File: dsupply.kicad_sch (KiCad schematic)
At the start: 67 parts, among them J5 Barrel_Jack, Q10 BC857, Q2 BSS138, Q3 BSS138, Q4 BC857, Q5 AOSP21321, Q6 BC857, Q8 BC857, Q9 AOSP21321, U21 ACPL-217-500E, U22 TPS54620, U24 PM1202, U25 AMS1117-3.3

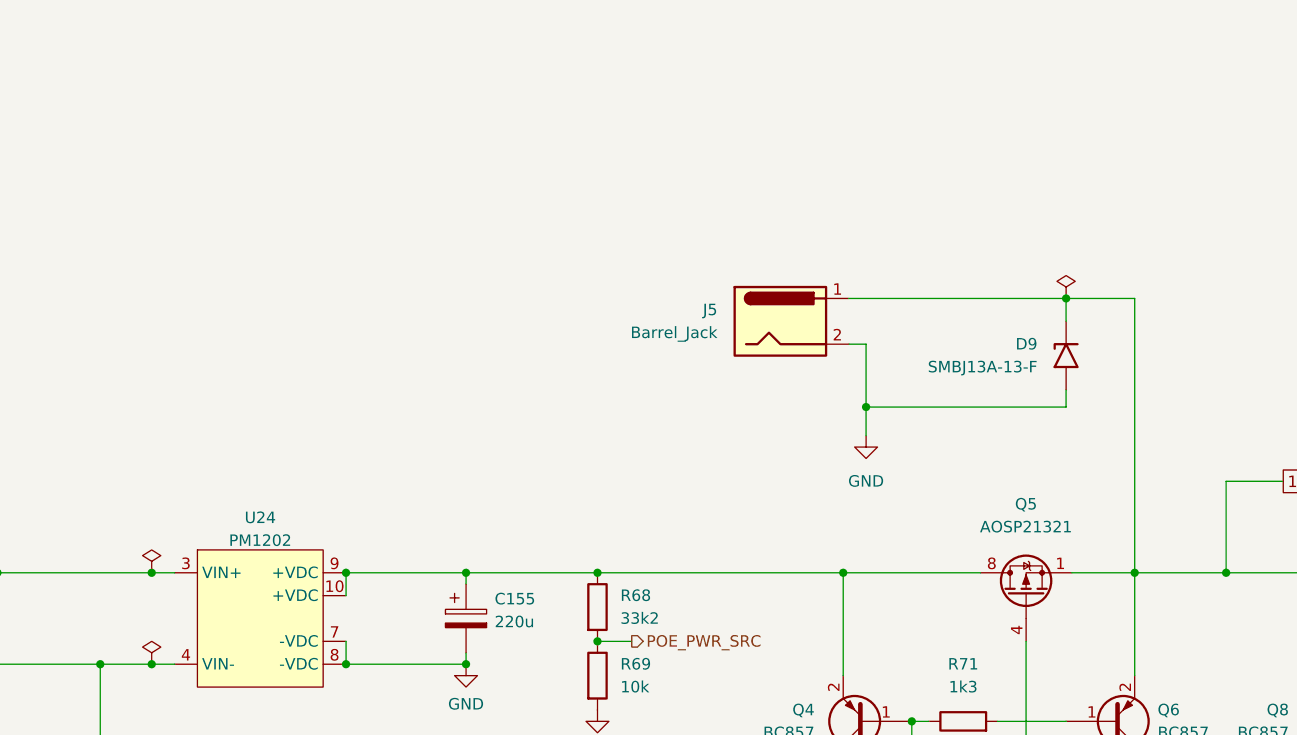
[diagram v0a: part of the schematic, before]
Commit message: sch: Add soft start to 12V PWR Jack input
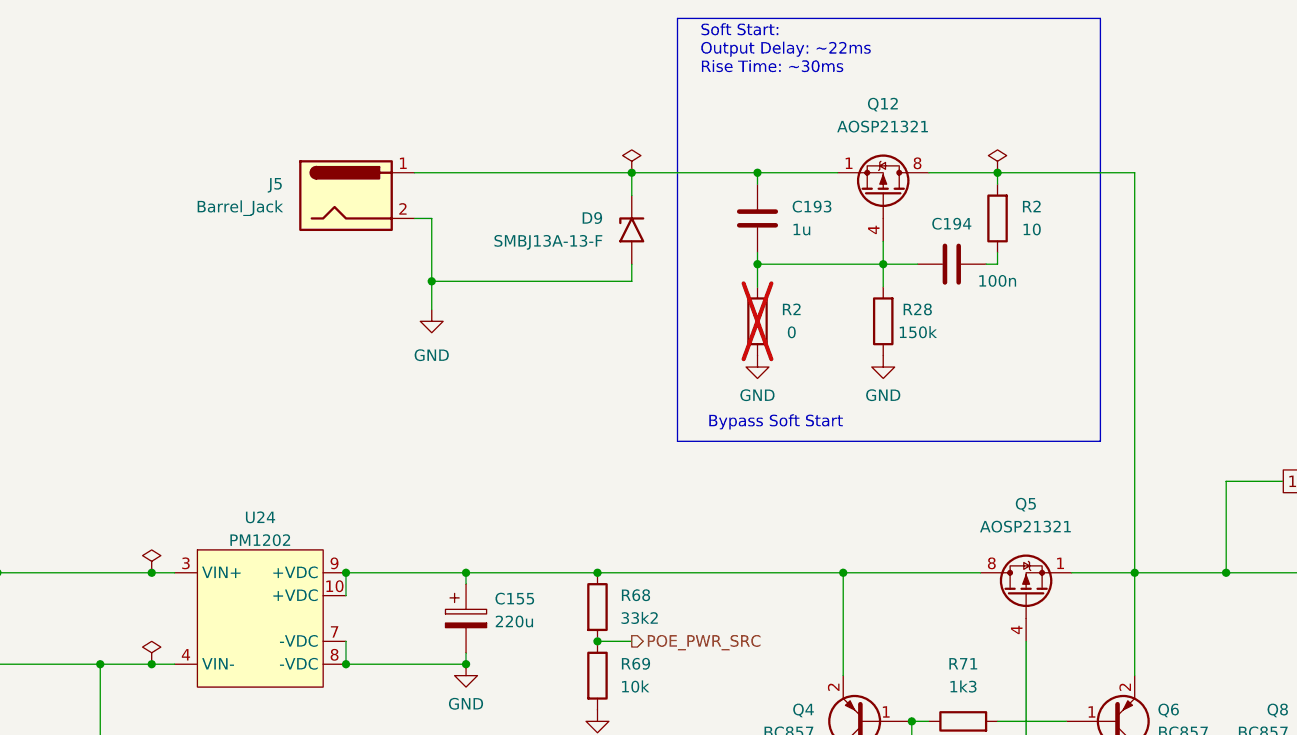
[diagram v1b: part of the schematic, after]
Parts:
- added C193: 1u, Capacitor_SMD:C_0603_1608Metric, symbol Device:C
- added C194: 100n, Capacitor_SMD:C_0603_1608Metric, symbol Device:C
- added Q12: AOSP21321, Package_SO:SOIC-8_3.9x4.9mm_P1.27mm, symbol Transistor_FET:FDS9435A
- added R2: 0, Resistor_SMD:R_0603_1608Metric, symbol Device:R
- added R2: 10, Resistor_SMD:R_0603_1608Metric, symbol Device:R
- added R28: 150k, Resistor_SMD:R_0603_1608Metric, symbol Device:R
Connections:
- net 12Vin: now also Q12.5 (D), Q12.6 (D), Q12.7 (D), Q12.8 (D), R2.2; no longer D9.1 (A1), J5.1
- net GND: now also R2.1, R28.1
- new net: C193.2, C194.1, Q12.4 (G), R2.2, R28.2
- new net: C193.1, D9.1 (A1), J5.1, Q12.1 (S), Q12.2 (S), Q12.3 (S)
- new net: C194.2, R2.1
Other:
- note added: "Bypass Soft Start"
- note added: "Soft Start: Output Delay: ~22ms Rise Time: ~30ms"
- moved on the sheet: D9, J5

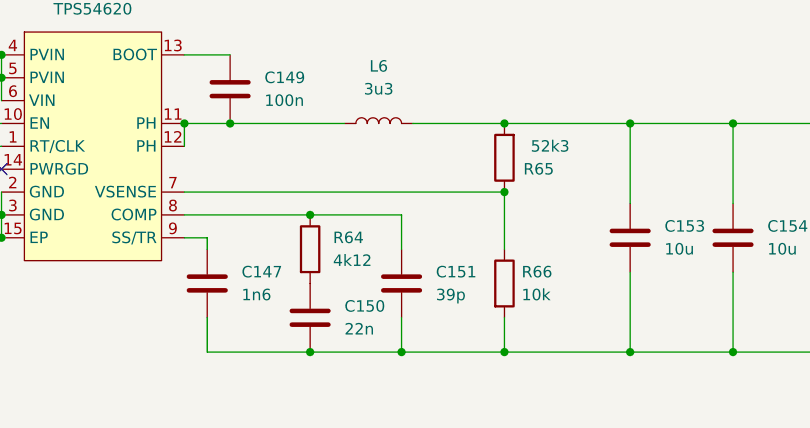
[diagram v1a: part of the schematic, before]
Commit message: sch: Modify dsupply freq_comp network - See Issue #21
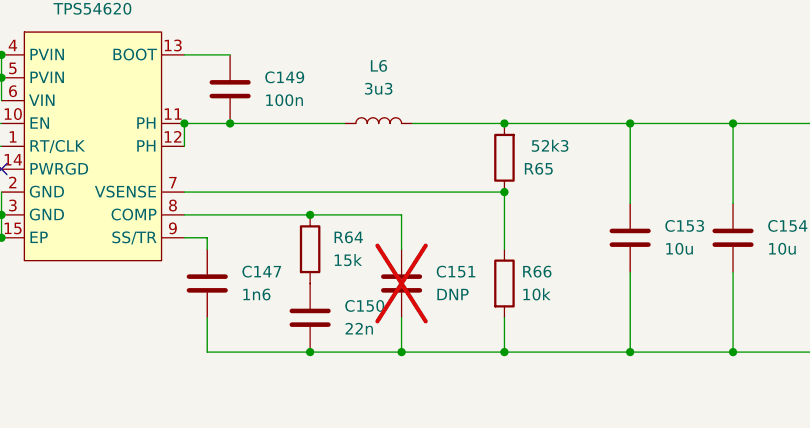
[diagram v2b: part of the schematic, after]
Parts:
- C151: value 39p -> DNP; MFR_PN 0603N390J500CT -> (none); now not fitted
- R64: value 4k12 -> 15k; MFR_PN RMCF0603FT4K12 -> (none); MFR_PN_ALT RC0603FR-074K12L -> (none)
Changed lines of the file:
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@@
       (effects (font (size 1.27 1.27)) (justify left))
     )
-    (property "Value" "4k12" (at 184.15 172.7199 0)
+    (property "Value" "15k" (at 184.15 172.7199 0)
       (effects (font (size 1.27 1.27)) (justify left))
     )
@@
       (effects (font (size 1.27 1.27)) hide)
     )
-    (property "MFR_PN" "RMCF0603FT4K12" (at 181.61 171.45 0)
-      (effects (font (size 1.27 1.27)) hide)
-    )
-    (property "MFR_PN_ALT" "RC0603FR-074K12L" (at 181.61 171.45 0)
+    (property "MFR_PN" "" (at 181.61 171.45 0)
+      (effects (font (size 1.27 1.27)) hide)
+    )
+    (property "MFR_PN_ALT" "" (at 181.61 171.45 0)
       (effects (font (size 1.27 1.27)) hide)
     )
@@
   )
   (symbol (lib_id "Device:C") (at 191.77 175.26 0) (unit 1)
-    (in_bom yes) (on_board yes) (dnp no) (fields_autoplaced)
+    (in_bom yes) (on_board yes) (dnp yes) (fields_autoplaced)
     (property "Reference" "C151" (at 195.58 173.9899 0)
       (effects (font (size 1.27 1.27)) (justify left))
     )
-    (property "Value" "39p" (at 195.58 176.5299 0)
+    (property "Value" "DNP" (at 195.58 176.5299 0)
       (effects (font (size 1.27 1.27)) (justify left))
     )
@@
       (effects (font (size 1.27 1.27)) hide)
     )
-    (property "MFR_PN" "0603N390J500CT" (at 191.77 175.26 0)
-      (effects (font (size 1.27 1.27)) hide)
-    )
+    (property "MFR_PN" "" (at 191.77 175.26 0)
+      (effects (font (size 1.27 1.27)) hide)
+    )

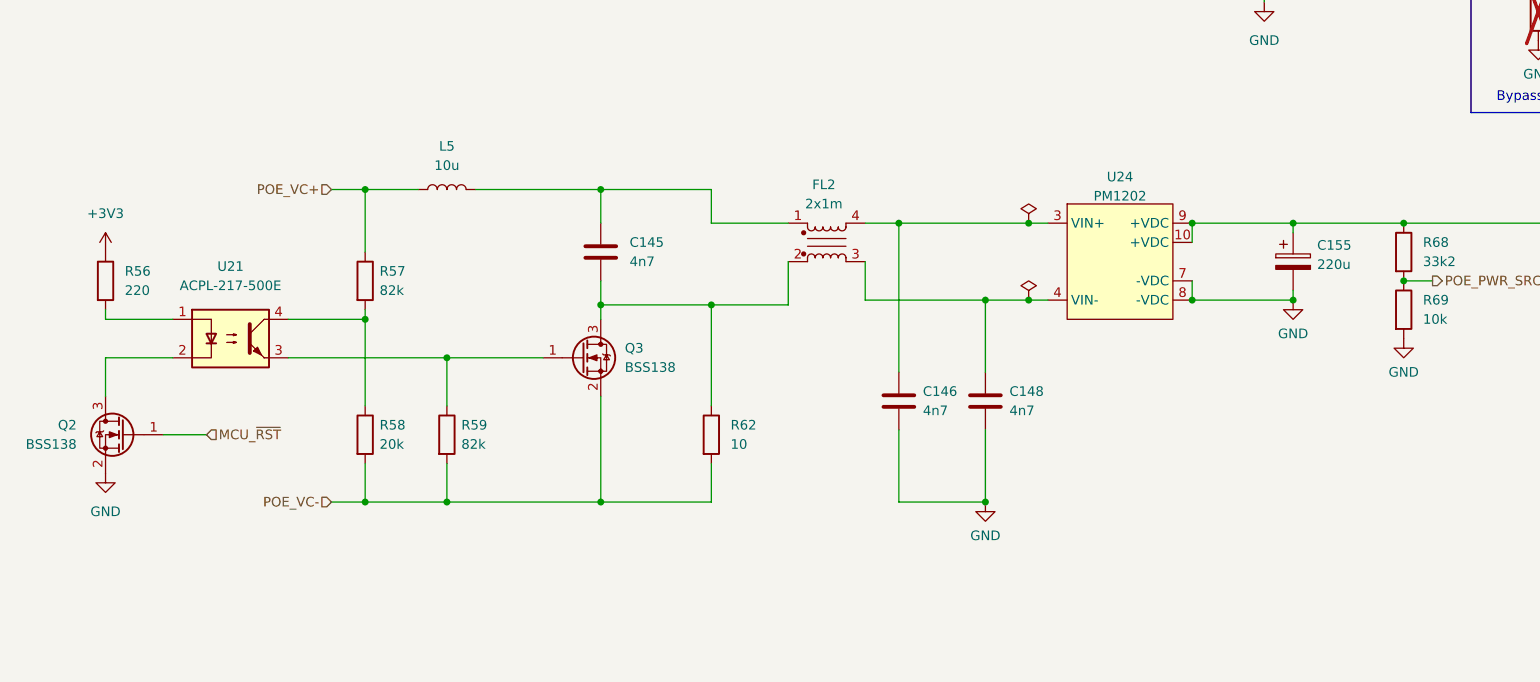
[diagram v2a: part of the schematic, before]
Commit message: sch: Change PoE RJ45 Jack and change PM1202 Symbol - Use the same PoE RJ45 as sinara-hw thermostat - Add PM1202 Power input pins (VB+, VB-) - Remove PoE softstart circuit as PM1202 has inrush current limiting - Add Pi Filter at the output of PM1202
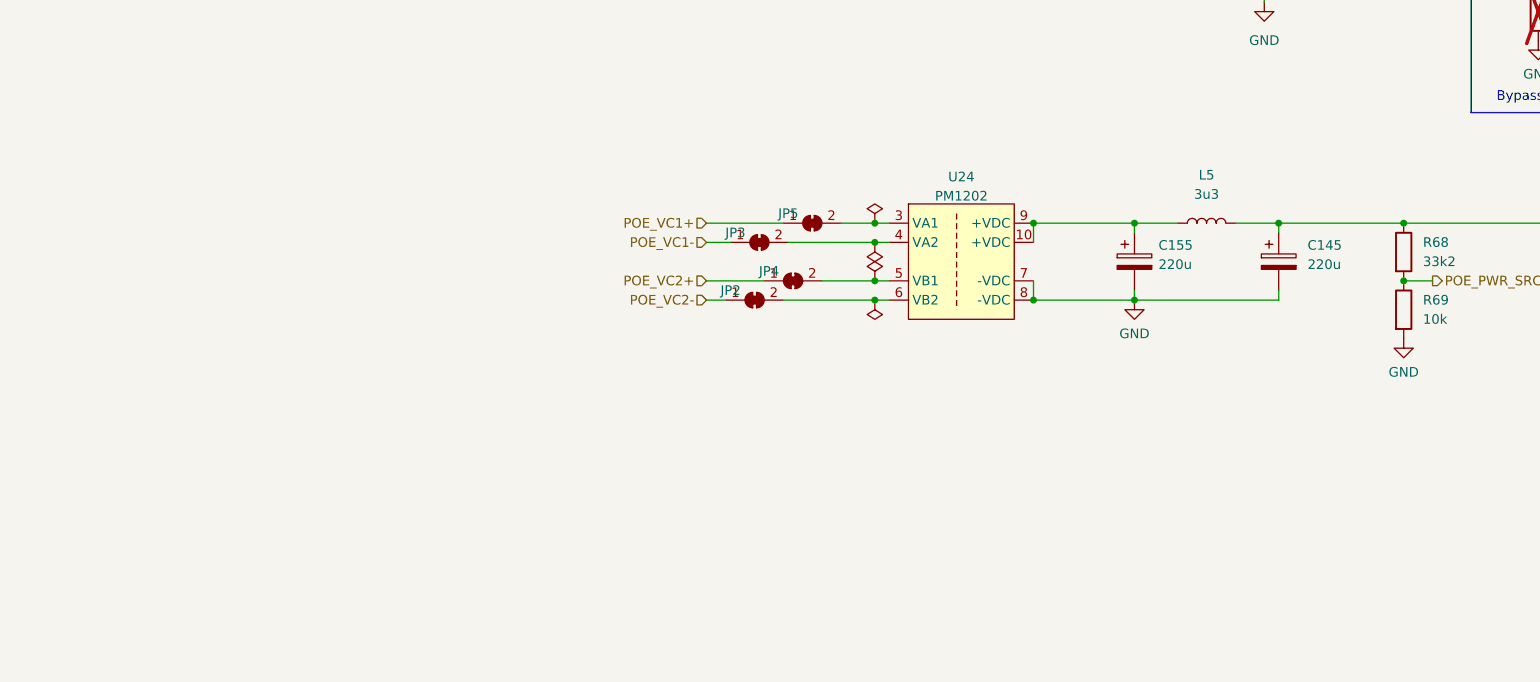
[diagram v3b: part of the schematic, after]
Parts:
- removed C145, C146, C148: 4n7, Capacitor_SMD:C_1206_3216Metric, symbol Device:C
- removed FL2: 2x1m, Inductor_SMD:L_CommonModeChoke_Wuerth_WE-SL5, symbol Device:Filter_EMI_LL_1423
- removed Q2, Q3: BSS138, Package_TO_SOT_SMD:SOT-23, symbol Transistor_FET:BSS138
- removed R56: 220, Resistor_SMD:R_0603_1608Metric, symbol Device:R
- removed R57, R59: 82k, Resistor_SMD:R_0603_1608Metric, symbol Device:R
- removed R58: 20k, Resistor_SMD:R_0603_1608Metric, symbol Device:R
- removed R62: 10, Resistor_SMD:R_0603_1608Metric, symbol Device:R
- removed U21: ACPL-217-500E, Package_DIP:SMDIP-4_W7.62mm, symbol Isolator:SFH617A-2X009T
- added C145: 220u, Capacitor_Tantalum_SMD:CP_EIA-7343-15_Kemet-W, symbol Device:C_Polarized
- added JP2, JP3, JP4, JP5: SolderJumper_2_Bridged, Jumper:SolderJumper-2_P1.3mm_Bridged2Bar_Pad1.0x1.5mm, symbol Jumper:SolderJumper_2_Bridged
- L5: value 10u -> 3u3; footprint Inductor_SMD:L_Wuerth_WE-PD-Typ-LS -> Inductor_SMD:L_Wuerth_MAPI-4020; MFR_PN 74477110 -> 74438356033
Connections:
- net GND: now also C145.2
- net at L5.2: now also Q4.2 (E), Q5.5 (D), Q5.6 (D), Q5.7 (D), Q5.8 (D), R68.1, C145.1
- net at U24.3 (VA1): now also JP5.2 (B)
- net at U24.4 (VA2): now also JP3.2 (B)
- net at U24.5 (VB1): now also JP4.2 (B)
- net at U24.6 (VB2): now also JP2.2 (B)
- net POE_VC+: no longer names the net of L5.1
- net POE_VC+: now also C155.1, U24.10 (+VDC), U24.9 (+VDC)
- new net POE_VC1+: JP5.1 (A)
- new net POE_VC1-: JP3.1 (A)
- new net POE_VC2+: JP4.1 (A)
- new net POE_VC2-: JP2.1 (A)
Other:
- moved on the sheet: C155

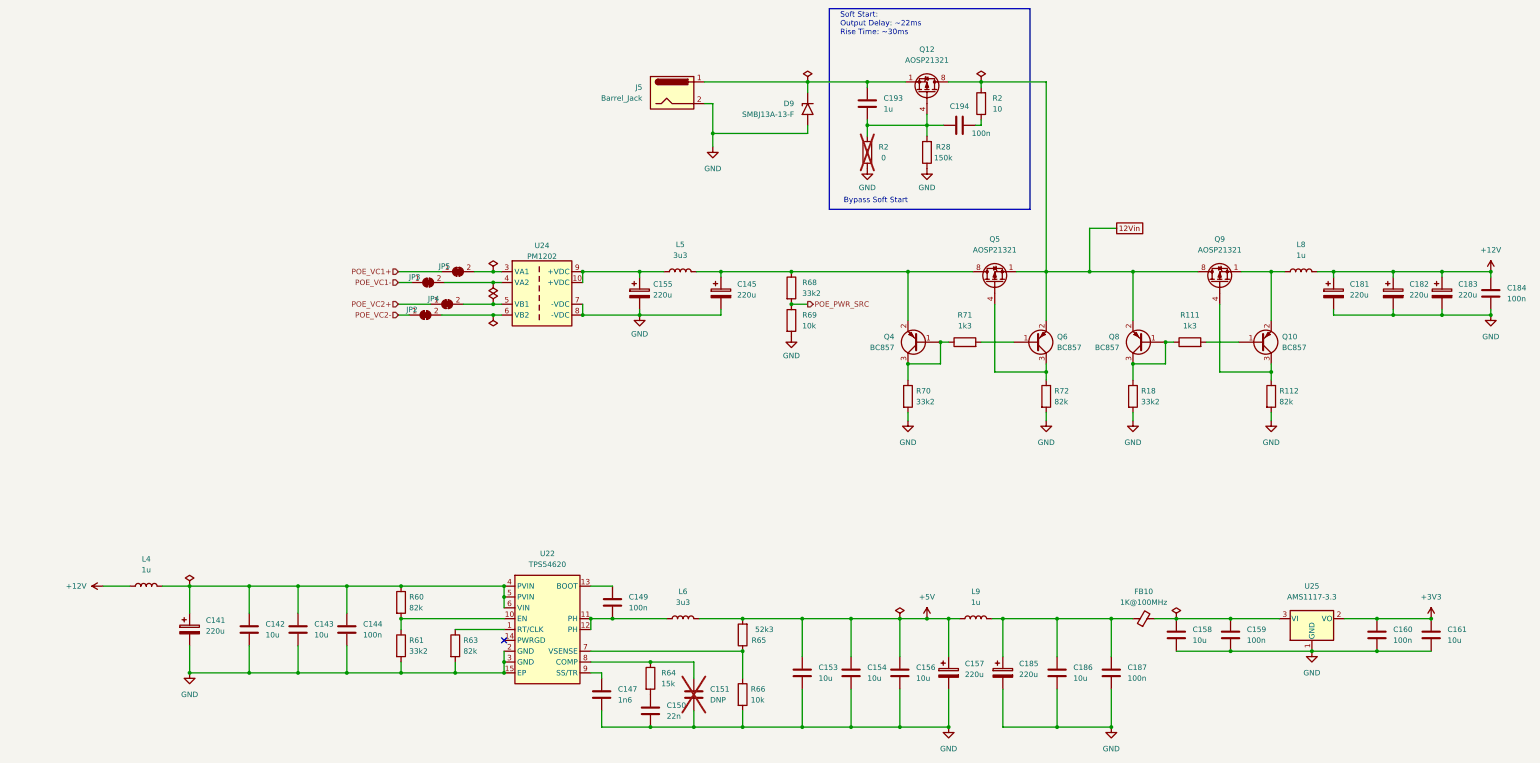
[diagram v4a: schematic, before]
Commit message: pcb: Finish Layout for rev0_3 - Assign MFR_PN for all Components - schematics changes:   - drivestage: Add Switch to optionally enable Modulation Signal Termination   -             Add alternate Precision Power Resistor   -             Modify the RC network values at TIA LPF Output   - MCU: Add Redundant 2.54mm pitch Programming Header   - thermostat: Duplicate the power filter network for alternate Temperature ADC
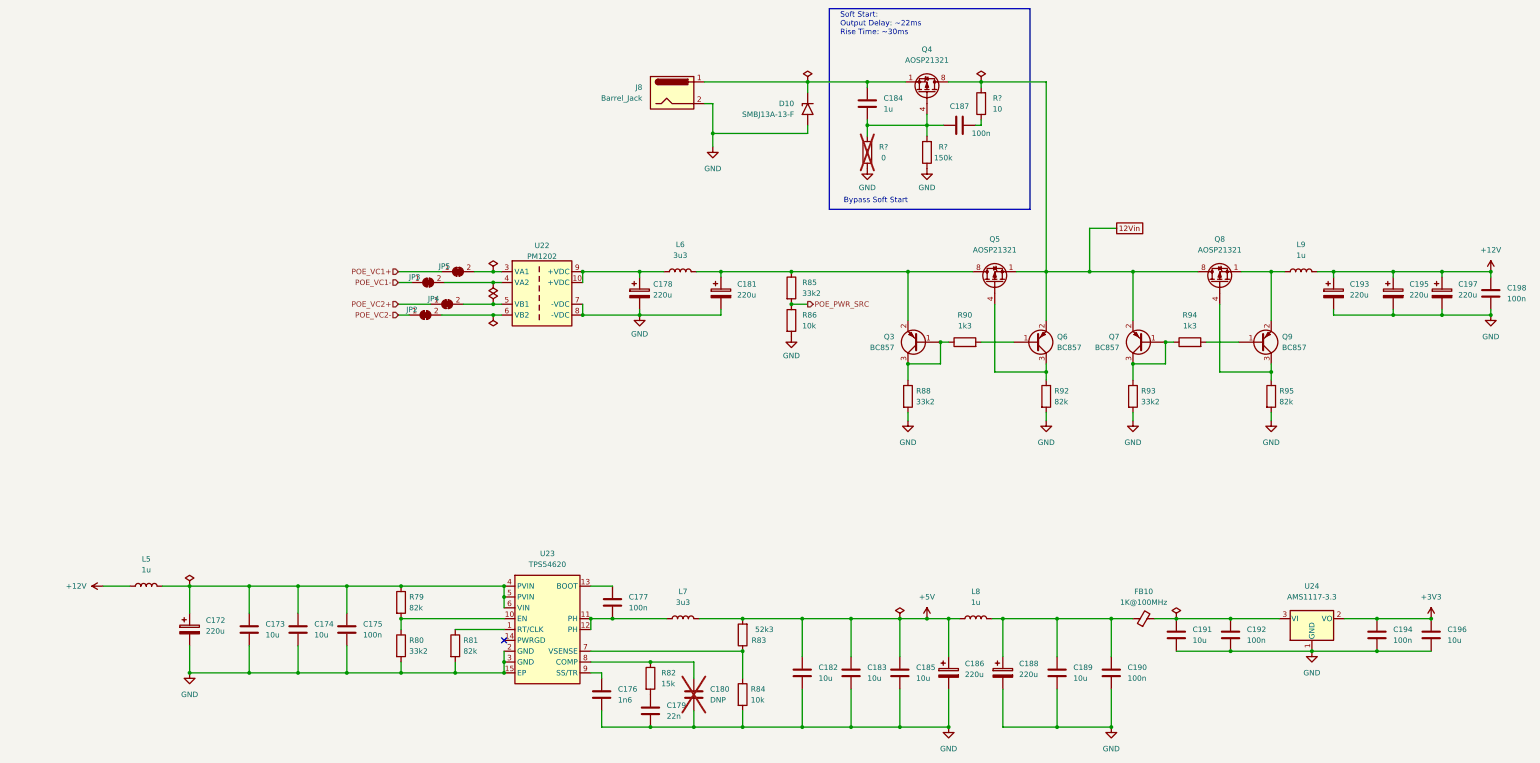
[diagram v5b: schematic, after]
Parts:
- C180: renamed from C151; MFR_PN_ALT CML0603C0G390JT50V -> (none)
- C187: renamed from C194; MFR_PN (none) -> CL10B104KB8NNWC; MFR_PN_ALT 0603B223J250CT -> CL10B104KB8NNNL
- R82: renamed from R64; MFR_PN (none) -> RT0603FRE0715KL
- R?: renamed from R2; MFR_PN (none) -> RMCF0603ZT0R00; MFR_PN_ALT WR06X10R0FTL -> CR0603-J/-000ELF
- R?: renamed from R2; MFR_PN (none) -> RT0603BRD0710RL
- U22: renamed from U24; MFR_PN (none) -> PM1202
- renumbered C141 to C172, C142 to C173, C143 to C174, C144 to C175, C147 to C176, C149 to C177, C155 to C178, C150 to C179, C145 to C181, C153 to C182, C154 to C183, C193 to C184, C156 to C185, C157 to C186, C185 to C188, C186 to C189, C187 to C190, C158 to C191, C159 to C192, C181 to C193, C160 to C194, C182 to C195, C161 to C196, C183 to C197, C184 to C198, D9 to D10, J5 to J8, L4 to L5, L5 to L6, L6 to L7, L9 to L8, L8 to L9, Q4 to Q3, Q12 to Q4, Q8 to Q7, Q9 to Q8, Q10 to Q9, R60 to R79, R61 to R80, R63 to R81, R65 to R83, R66 to R84, R68 to R85, R69 to R86, R70 to R88, R71 to R90, R72 to R92, R18 to R93, R111 to R94, R112 to R95, R28 to R?, U22 to U23, U25 to U24

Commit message: sch, pcb: exclude MHs and soldering JP from BOM
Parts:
- JP2, JP3, JP4, JP5: now left out of the parts list
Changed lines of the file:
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@@
   )
   (symbol (lib_id "Jumper:SolderJumper_2_Bridged") (at 136.525 76.2 0) (unit 1)
-    (in_bom yes) (on_board yes) (dnp no)
+    (in_bom no) (on_board yes) (dnp no)
     (property "Reference" "JP5" (at 133.35 74.93 0)
       (effects (font (size 1.27 1.27)))
@@
   )
   (symbol (lib_id "Jumper:SolderJumper_2_Bridged") (at 128.905 86.36 0) (unit 1)
-    (in_bom yes) (on_board yes) (dnp no)
+    (in_bom no) (on_board yes) (dnp no)
     (property "Reference" "JP2" (at 125.73 85.09 0)
       (effects (font (size 1.27 1.27)))
@@
   )
   (symbol (lib_id "Jumper:SolderJumper_2_Bridged") (at 133.985 83.82 0) (unit 1)
-    (in_bom yes) (on_board yes) (dnp no)
+    (in_bom no) (on_board yes) (dnp no)
     (property "Reference" "JP4" (at 130.81 82.55 0)
       (effects (font (size 1.27 1.27)))
@@
   )
   (symbol (lib_id "Jumper:SolderJumper_2_Bridged") (at 129.54 78.74 0) (unit 1)
-    (in_bom yes) (on_board yes) (dnp no)
+    (in_bom no) (on_board yes) (dnp no)
     (property "Reference" "JP3" (at 126.365 77.47 0)
       (effects (font (size 1.27 1.27)))

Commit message: sch: Update Title Block Info - rev0.3 -> rev0_3 - Correct the title of each schematics - Update the modified time
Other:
- company: M-Labs -> M-Labs Limited
- title: Kirdy -> digital supply
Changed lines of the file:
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@@
   (paper "A3")
   (title_block
-    (title "Kirdy")
-    (date "2022-07-03")
-    (rev "r0.3")
-    (company "M-Labs")
+    (title "digital supply")
+    (date "2023-11-09")
+    (rev "r0_3")
+    (company "M-Labs Limited")
     (comment 1 "Linus Woo Chun Kit")
   )
